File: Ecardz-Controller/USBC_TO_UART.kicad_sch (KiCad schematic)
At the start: 1 part, among them J3 USB_C_Receptacle_USB2.0_16P

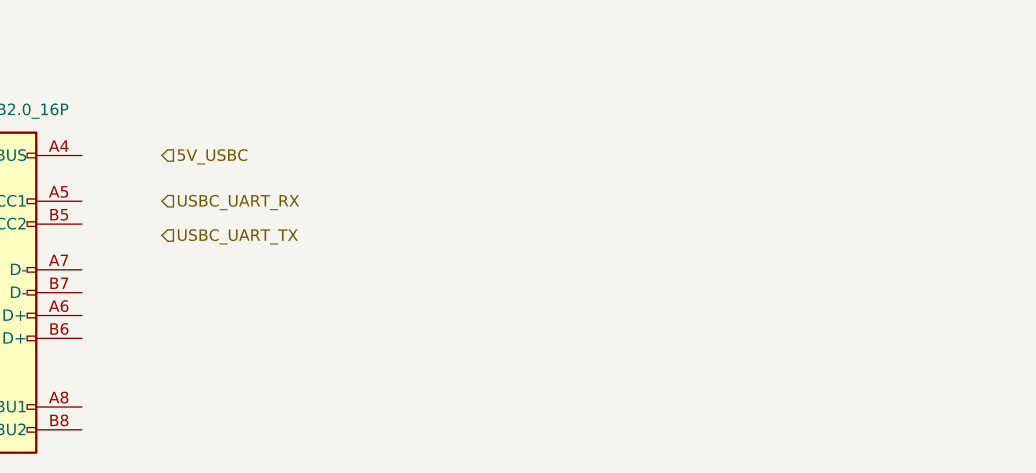
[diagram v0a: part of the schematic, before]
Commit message: adding MCU
added peripheral connections as well as indicator lights
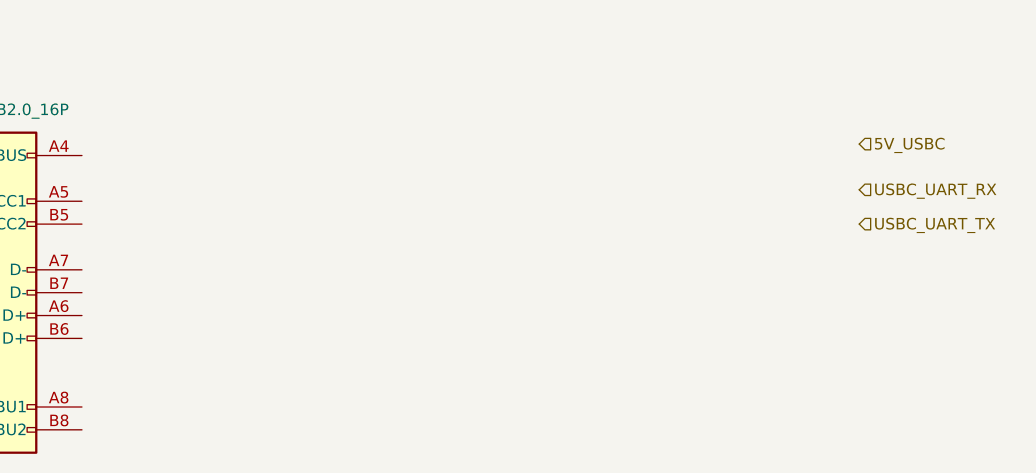
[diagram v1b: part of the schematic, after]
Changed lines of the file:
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@@
 	(hierarchical_label "USBC_UART_RX"
 		(shape input)
-		(at 55.88 38.1 0)
+		(at 133.35 36.83 0)
 		(fields_autoplaced yes)
 		(effects
@@
 	(hierarchical_label "USBC_UART_TX"
 		(shape input)
-		(at 55.88 41.91 0)
+		(at 133.35 40.64 0)
 		(fields_autoplaced yes)
 		(effects
@@
 	(hierarchical_label "5V_USBC"
 		(shape input)
-		(at 55.88 33.02 0)
+		(at 133.35 31.75 0)
 		(fields_autoplaced yes)
 		(effects

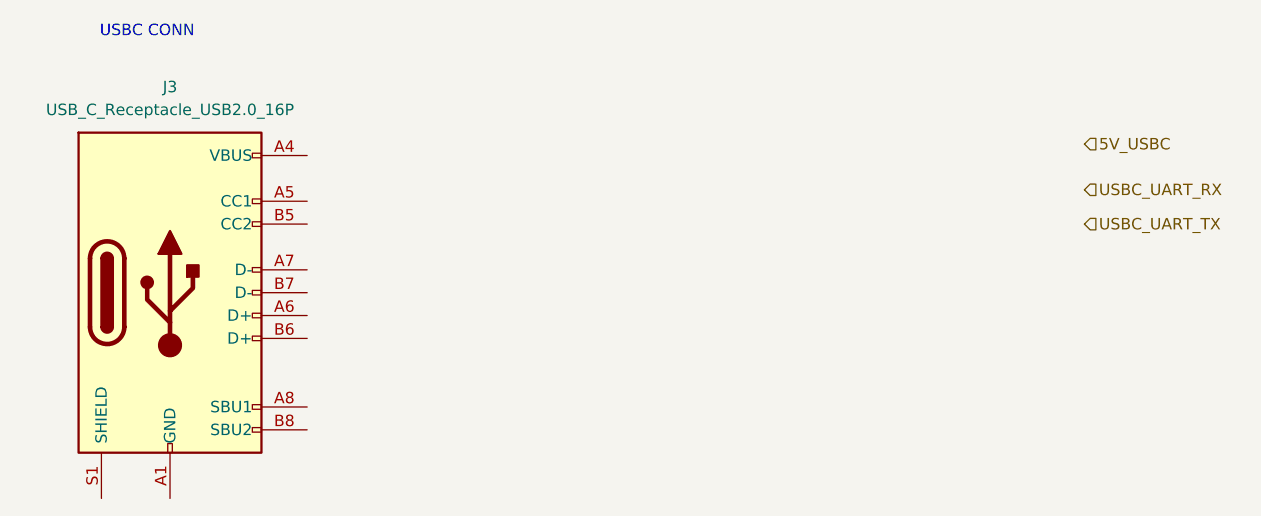
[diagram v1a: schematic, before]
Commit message: updated button pin choices, updated root
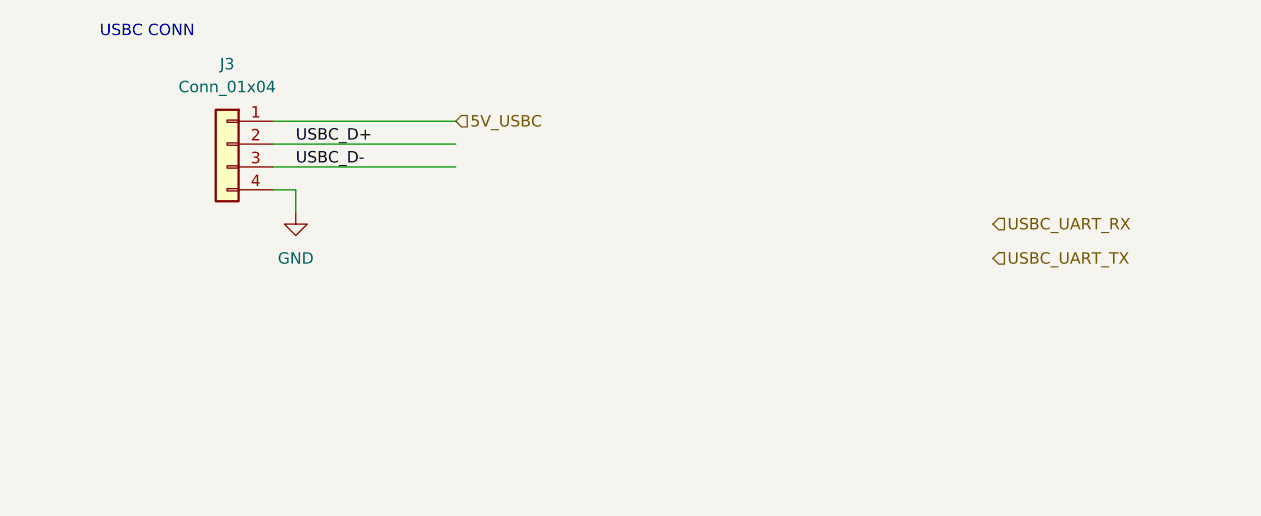
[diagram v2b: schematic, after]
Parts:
- removed J3: USB_C_Receptacle_USB2.0_16P, symbol Connector:USB_C_Receptacle_USB2.0_16P
- added J3: Conn_01x04, symbol Connector_Generic:Conn_01x04
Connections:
- net 5V_USBC: now also J3.1 (Pin_1)
- new net GND: J3.4 (Pin_4)
- new net USBC_D+: J3.2 (Pin_2)
- new net USBC_D-: J3.3 (Pin_3)
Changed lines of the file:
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@@
 	(generator_version "8.0")
 	(paper "A4")
+	(wire
+		(pts
+			(xy 45.72 36.83) (xy 45.72 39.37)
+		)
+		(stroke
+			(width 0)
+			(type default)
+		)
+	)
+	(wire
+		(pts
+			(xy 43.18 31.75) (xy 63.5 31.75)
+		)
+		(stroke
+			(width 0)
+			(type default)
+		)
+	)
+	(wire
+		(pts
+			(xy 43.18 36.83) (xy 45.72 36.83)
+		)
+		(stroke
+			(width 0)
+			(type default)
+		)
+	)
+	(wire
+		(pts
+			(xy 43.18 29.21) (xy 63.5 29.21)
+		)
+		(stroke
+			(width 0)
+			(type default)
+		)
+	)
+	(wire
+		(pts
+			(xy 43.18 34.29) (xy 63.5 34.29)
+		)
+		(stroke
+			(width 0)
+			(type default)
+		)
+	)
 	(text "USBC CONN\n"
 		(exclude_from_sim no)
@@
 		)
 	)
+	(label "USBC_D-"
+		(at 45.72 34.29 0)
+		(fields_autoplaced yes)
+		(effects
+			(font
+				(size 1.27 1.27)
+			)
+			(justify left bottom)
+		)
+	)
+	(label "USBC_D+"
+		(at 45.72 31.75 0)
+		(fields_autoplaced yes)
+		(effects
+			(font
+				(size 1.27 1.27)
+			)
+			(justify left bottom)
+		)
+	)
 	(hierarchical_label "USBC_UART_RX"
 		(shape input)
-		(at 133.35 36.83 0)
+		(at 123.19 40.64 0)
 		(fields_autoplaced yes)
 		(effects
@@
 	(hierarchical_label "USBC_UART_TX"
 		(shape input)
-		(at 133.35 40.64 0)
+		(at 123.19 44.45 0)
 		(fields_autoplaced yes)
 		(effects
@@
 	(hierarchical_label "5V_USBC"
 		(shape input)
-		(at 133.35 31.75 0)
+		(at 63.5 29.21 0)
 		(fields_autoplaced yes)
 		(effects
@@
 	)
 	(symbol
-		(lib_id "Connector:USB_C_Receptacle_USB2.0_16P")
-		(at 31.75 48.26 0)
+		(lib_id "power:GND")
+		(at 45.72 39.37 0)
 		(unit 1)
 		(exclude_from_sim no)
@@
 		(dnp no)
 		(fields_autoplaced yes)
+		(property "Reference" "#PWR011"
+			(at 45.72 45.72 0)
+			(effects
+				(font
+					(size 1.27 1.27)
+				)
+				(hide yes)
+			)
+		)
+		(property "Value" "GND"
+			(at 45.72 44.45 0)
+			(effects
+				(font
+					(size 1.27 1.27)
+				)
+			)
+		)
+		(property "Footprint" ""
+			(at 45.72 39.37 0)
+			(effects
+				(font
+					(size 1.27 1.27)
+				)
+				(hide yes)
+			)
+		)
+		(property "Datasheet" ""
+			(at 45.72 39.37 0)
+			(effects
+				(font
+					(size 1.27 1.27)
+				)
+				(hide yes)
+			)
+		)
+		(property "Description" "Power symbol creates a global label with name \"GND\" , ground"
+			(at 45.72 39.37 0)
+			(effects
+				(font
+					(size 1.27 1.27)
+				)
+				(hide yes)
+			)
+		)
+		(pin "1"
+		)
+		(instances
+			(project "Ecardz-Controller"
+				(path "/74270717-a116-451e-ac88-5a07ab66056e/795903a0-6fb6-4696-956b-ef2670233793"
+					(reference "#PWR011")
+					(unit 1)
+				)
+			)
+		)
+	)
+	(symbol
+		(lib_id "Connector_Generic:Conn_01x04")
+		(at 38.1 31.75 0)
+		(mirror y)
+		(unit 1)
+		(exclude_from_sim no)
+		(in_bom yes)
+		(on_board yes)
+		(dnp no)
+		(fields_autoplaced yes)
 		(property "Reference" "J3"
-			(at 31.75 25.4 0)
-			(effects
-				(font
-					(size 1.27 1.27)
-				)
-			)
-		)
-		(property "Value" "USB_C_Receptacle_USB2.0_16P"
-			(at 31.75 27.94 0)
+			(at 38.1 22.86 0)
+			(effects
+				(font
+					(size 1.27 1.27)
+				)
+			)
+		)
+		(property "Value" "Conn_01x04"
+			(at 38.1 25.4 0)
 			(effects
 				(font
@@
 		)
 		(property "Footprint" ""
-			(at 35.56 48.26 0)
-			(effects
-				(font
-					(size 1.27 1.27)
-				)
-				(hide yes)
-			)
-		)
-		(property "Datasheet" "https://www.usb.org/sites/default/files/documents/usb_type-c.zip"
-			(at 35.56 48.26 0)
-			(effects
-				(font
-					(size 1.27 1.27)
-				)
-				(hide yes)
-			)
-		)
-		(property "Description" "USB 2.0-only 16P Type-C Receptacle connector"
-			(at 31.75 48.26 0)
-			(effects
-				(font
-					(size 1.27 1.27)
-				)
-				(hide yes)
-			)
-		)
-		(pin "B1"
-		)
-		(pin "B7"
-		)
-		(pin "A4"
-		)
-		(pin "A5"
-		)
-		(pin "A6"
-		)
-		(pin "A1"
-		)
-		(pin "A9"
-		)
-		(pin "B5"
-		)
-		(pin "B8"
-		)
-		(pin "B9"
-		)
-		(pin "S1"
-		)
-		(pin "A8"
-		)
-		(pin "A7"
-		)
-		(pin "A12"
-		)
-		(pin "B4"
-		)
-		(pin "B12"
-		)
-		(pin "B6"
+			(at 38.1 31.75 0)
+			(effects
+				(font
+					(size 1.27 1.27)
+				)
+				(hide yes)
+			)
+		)
+		(property "Datasheet" "~"
+			(at 38.1 31.75 0)
+			(effects
+				(font
+					(size 1.27 1.27)
+				)
+				(hide yes)
+			)
+		)
+		(property "Description" "Generic connector, single row, 01x04, script generated (kicad-library-utils/schlib/autogen/connector/)"
+			(at 38.1 31.75 0)
+			(effects
+				(font
+					(size 1.27 1.27)
+				)
+				(hide yes)
+			)
+		)
+		(pin "3"
+		)
+		(pin "2"
+		)
+		(pin "1"
+		)
+		(pin "4"
 		)
 		(instances

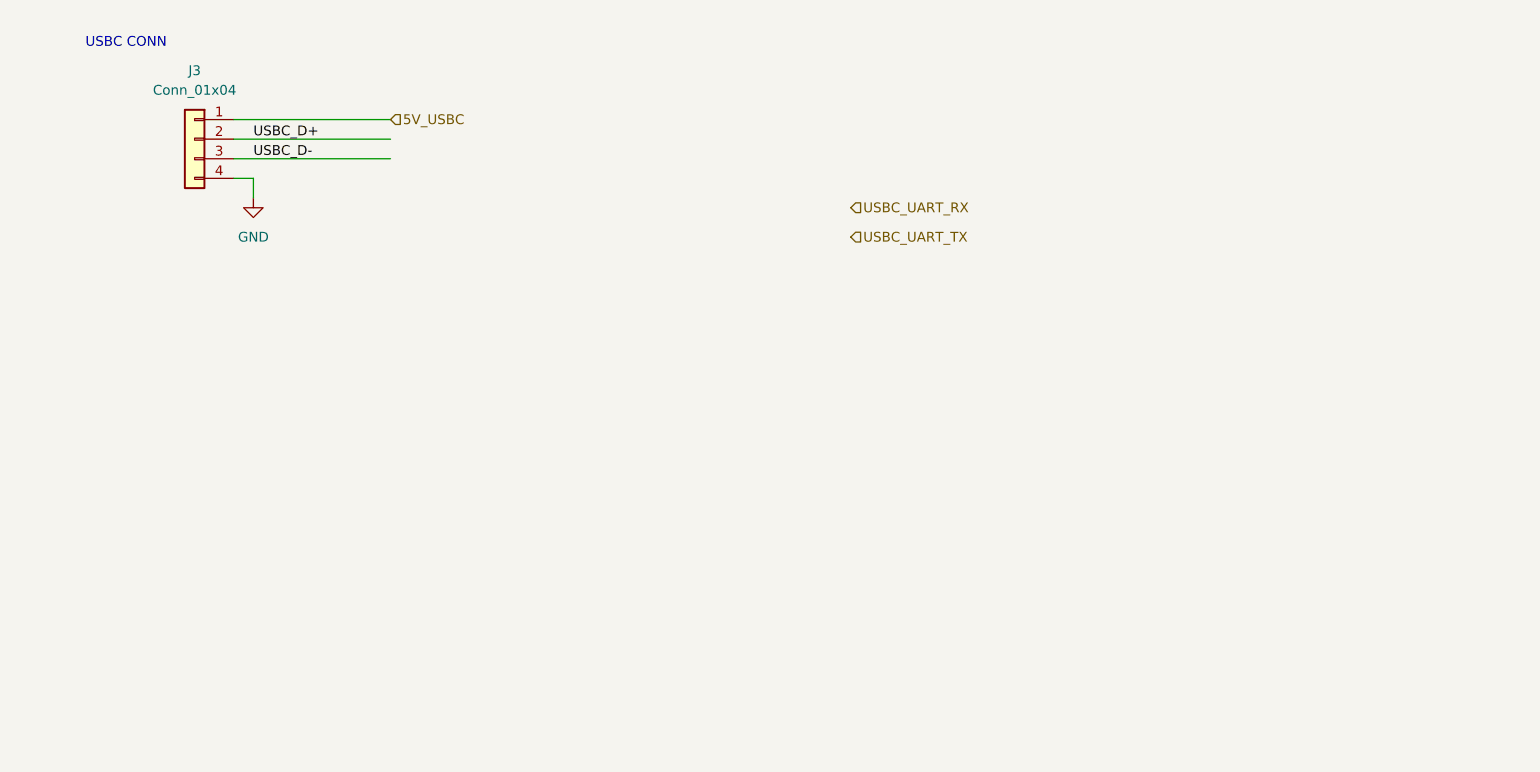
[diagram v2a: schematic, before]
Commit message: usb to uart chip
currently using the wrong kicad part number but they are footprint compatible
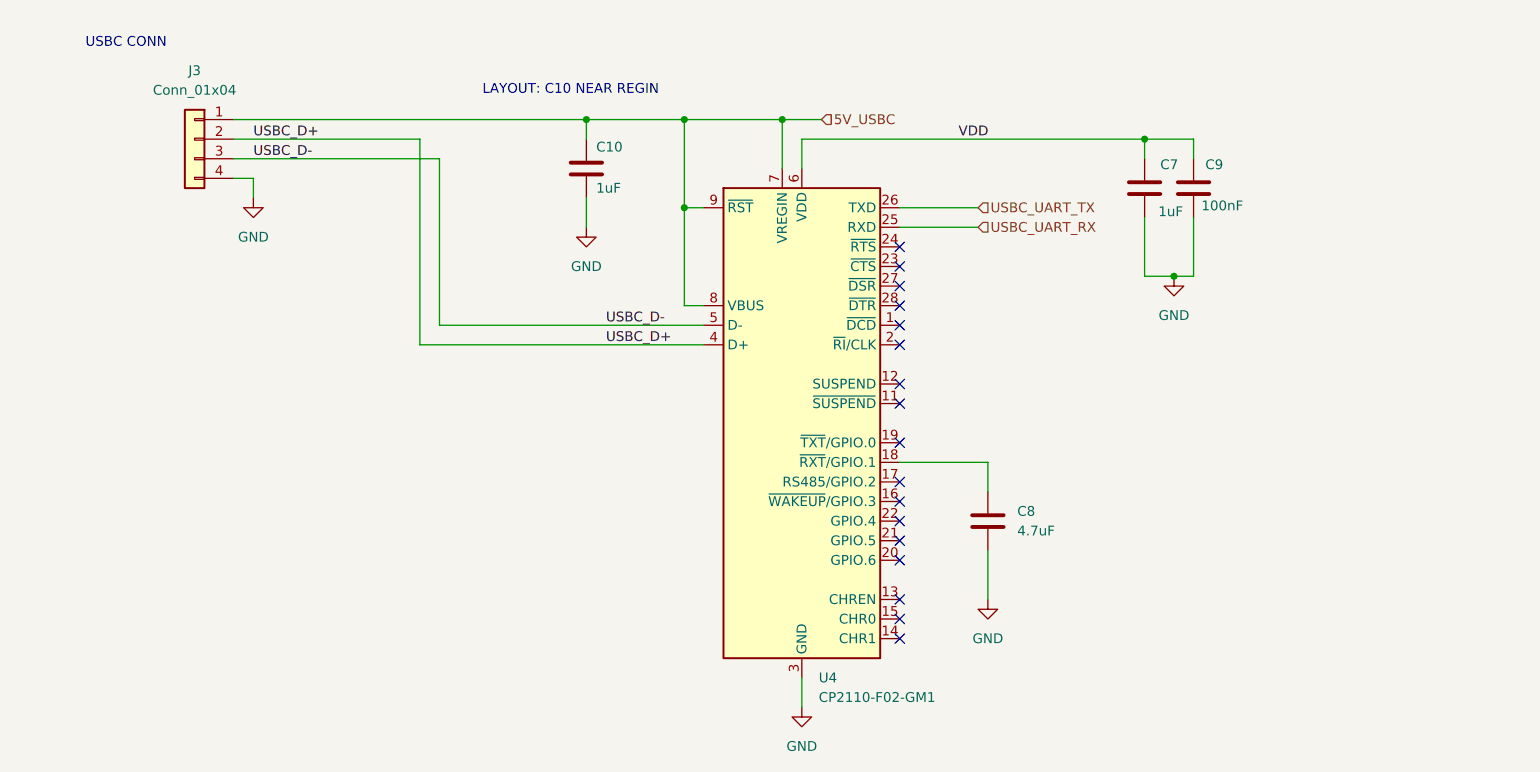
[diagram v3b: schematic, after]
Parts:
- added C10, C7: 1uF, Capacitor_SMD:C_0603_1608Metric_Pad1.08x0.95mm_HandSolder, symbol Device:C
- added C8: 4.7uF, Capacitor_SMD:C_0603_1608Metric_Pad1.08x0.95mm_HandSolder, symbol Device:C
- added C9: 100nF, Capacitor_SMD:C_0603_1608Metric_Pad1.08x0.95mm_HandSolder, symbol Device:C
- added U4: CP2110-F02-GM1, Package_DFN_QFN:QFN-28-1EP_5x5mm_P0.5mm_EP3.35x3.35mm, symbol Interface_USB:CP2102N-Axx-xQFN28
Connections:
- net 5V_USBC: now also C10.1, U4.7 (VREGIN), U4.8 (VBUS), U4.9 (~{RST})
- net GND: now also C10.2, C7.2, C8.2, C9.2, U4.29 (GND), U4.3 (GND)
- net USBC_D+: now also U4.4 (D+)
- net USBC_D-: now also U4.5 (D-)
- net USBC_UART_RX: now also U4.25 (RXD)
- net USBC_UART_TX: now also U4.26 (TXD)
- new net: C8.1, U4.18 (~{RXT}/GPIO.1)
- new net VDD: C7.1, C9.1, U4.6 (VDD)
- no-connect marks 0 -> 17
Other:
- note added: "LAYOUT: C10 NEAR REGIN"

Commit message: small updates
added 0 ohm on uart, more caps on power pins
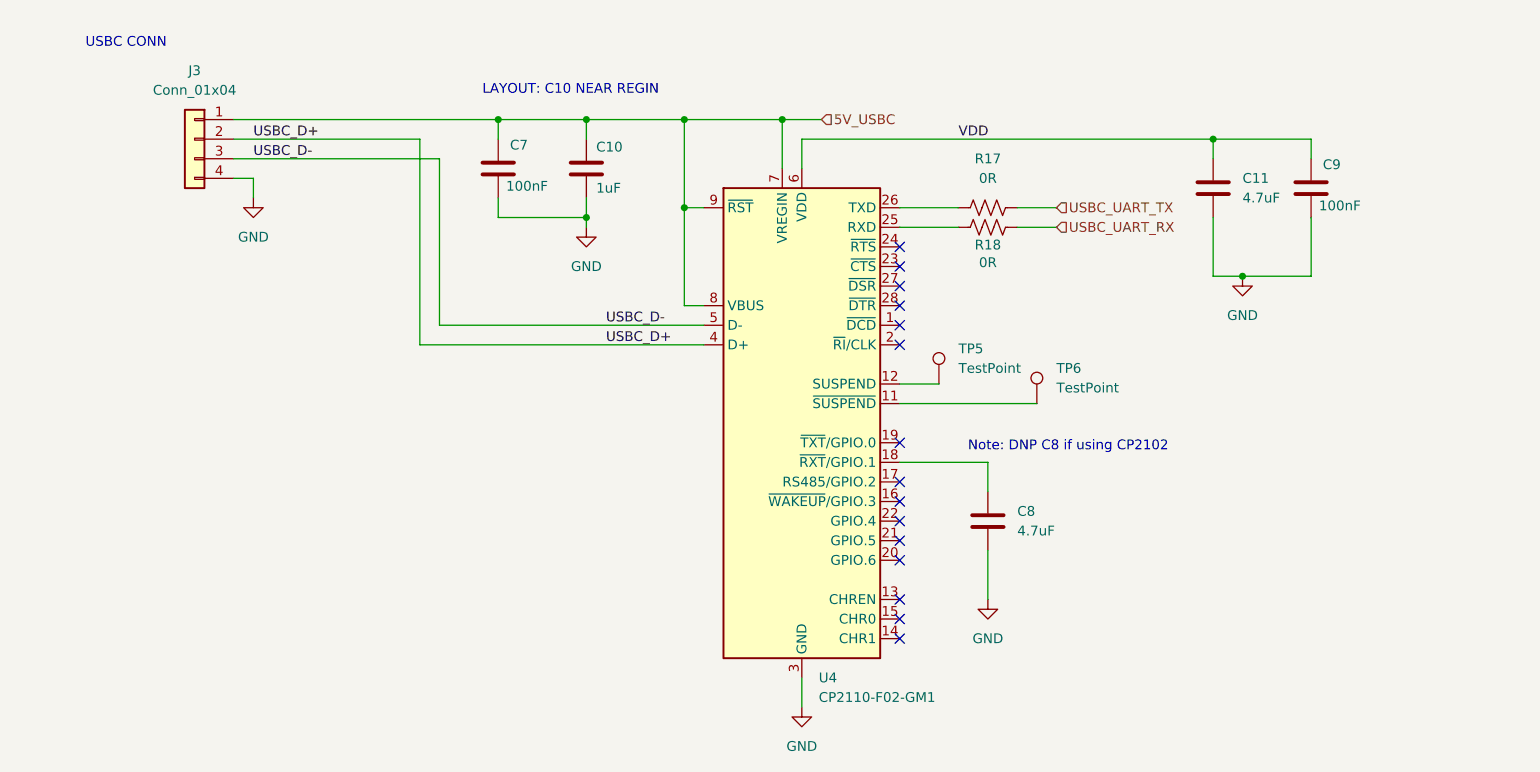
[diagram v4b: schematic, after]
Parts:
- added C11: 4.7uF, Capacitor_SMD:C_0603_1608Metric_Pad1.08x0.95mm_HandSolder, symbol Device:C
- added R17, R18: 0R, Resistor_SMD:R_0603_1608Metric_Pad0.98x0.95mm_HandSolder, symbol Device:R_US
- added TP5, TP6: TestPoint, TestPoint:TestPoint_Pad_D3.0mm, symbol Connector:TestPoint
- C7: value 1uF -> 100nF; Part Number CC0603KRX5R8BB105 -> CC0603KRX7R7BB104
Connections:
- net 5V_USBC: now also C7.1
- net GND: now also C11.2
- net USBC_UART_RX: now also R18.2; no longer U4.25 (RXD)
- net USBC_UART_TX: now also R17.2; no longer U4.26 (TXD)
- net VDD: now also C11.1; no longer C7.1
- net at U4.11 (~{SUSPEND}): now also TP6.1
- net at U4.12 (SUSPEND): now also TP5.1
- new net: R18.1, U4.25 (RXD)
- new net: R17.1, U4.26 (TXD)
- no-connect marks 17 -> 15
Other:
- note added: "Note: DNP C8 if using CP2102"
- moved on the sheet: C9
